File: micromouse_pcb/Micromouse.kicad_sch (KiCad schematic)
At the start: 83 parts, among them J1 Conn_01x06, J2 Conn_01x06, J3 SWD, J4 UART, Q1 NMOS, Q2 SFH300, Q3 SFH300, Q4 NMOS, Q5 SFH300, Q6 NMOS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

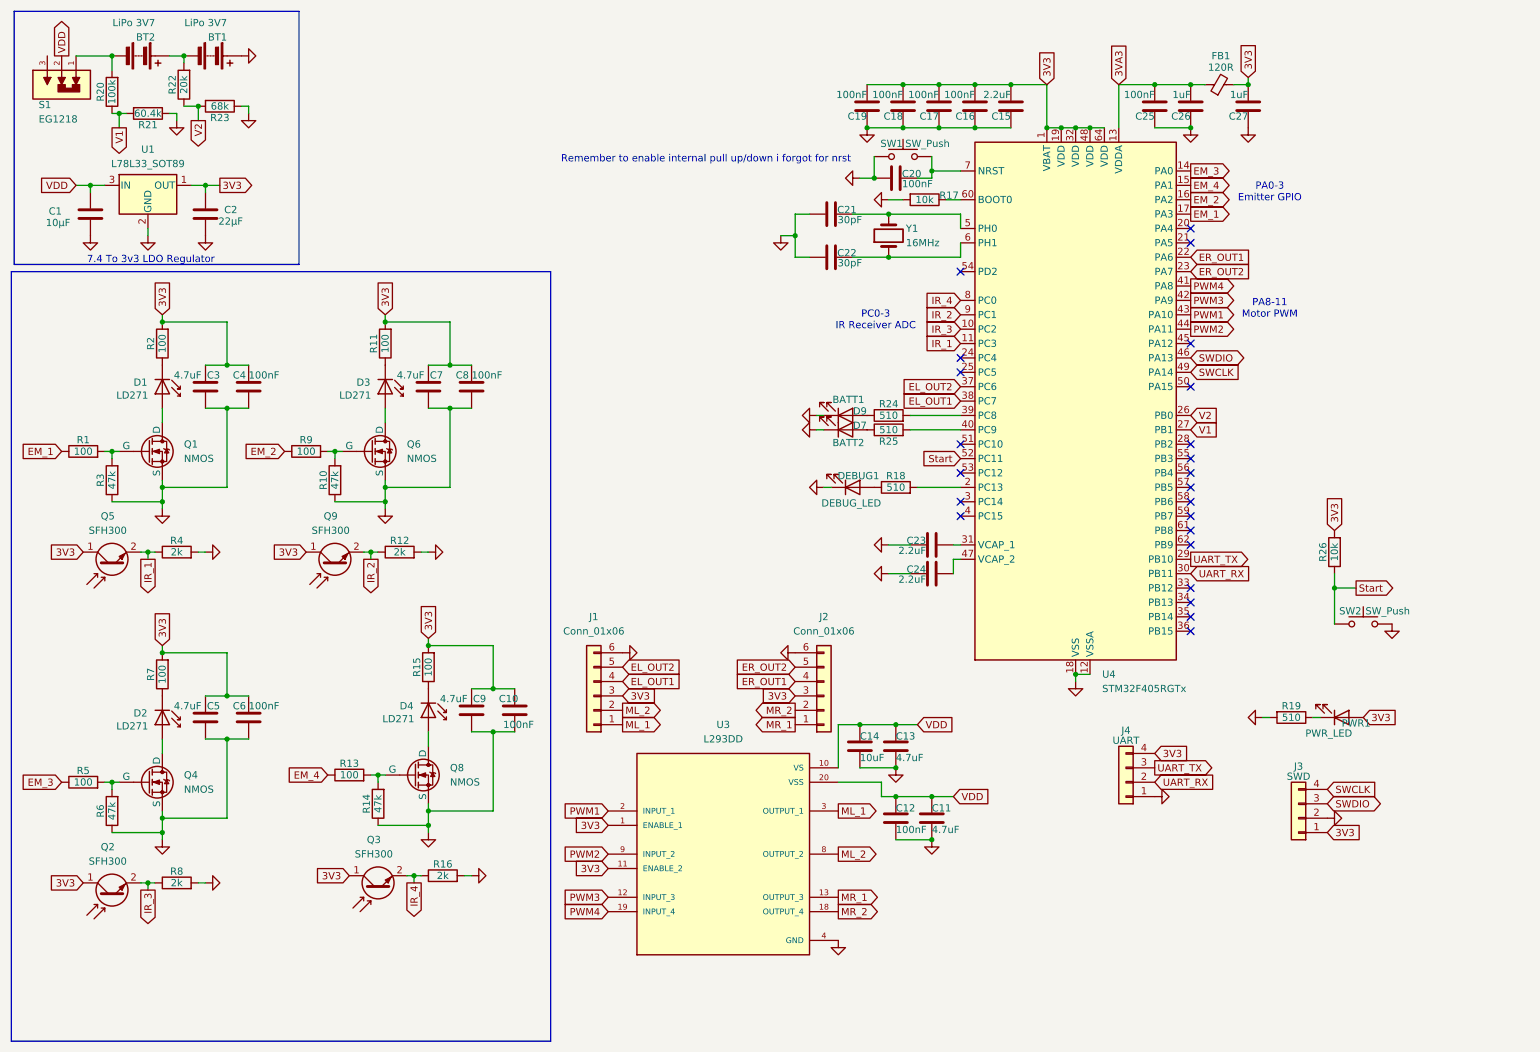
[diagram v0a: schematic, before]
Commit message: v2 kicad micromouse started, and turning is now possible but please fix distance reading and distance pids
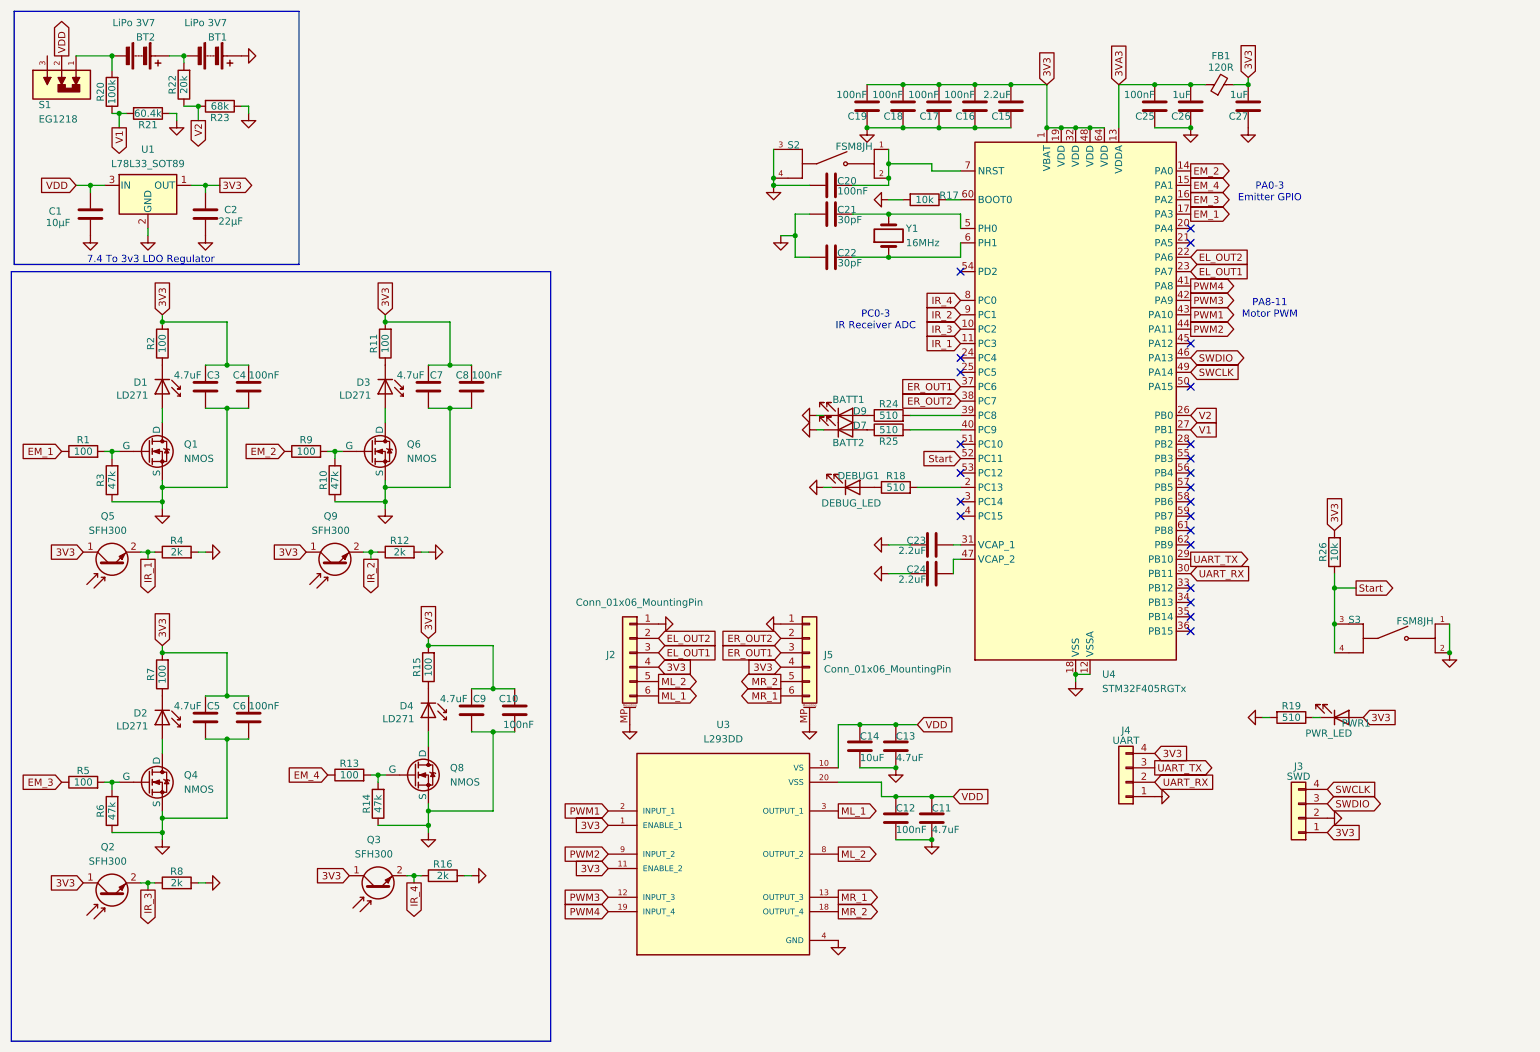
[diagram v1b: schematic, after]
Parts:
- removed J1, J2: Conn_01x06, Connector_JST:JST_SH_BM06B-SRSS-TB_1x06-1MP_P1.00mm_Vertical, symbol Connector_Generic:Conn_01x06
- removed SW1, SW2: SW_Push, footprints:SW4_1825910-B_TEC, symbol Switch:SW_Push
- added J2, J5: Conn_01x06_MountingPin, Connector_JST:JST_SH_BM06B-SRSS-TB_1x06-1MP_P1.00mm_Vertical, symbol Connector_Generic_MountingPin:Conn_01x06_MountingPin
- added S2, S3: FSM8JH, footprints:SW4_1825910-B_TEC, symbol FSM8JH:FSM8JH
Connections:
- net 3V3: now also J2.4 (Pin_4), J5.4 (Pin_4)
- net EL_OUT1: now also U4.23 (PA7), J2.3 (Pin_3); no longer U4.38 (PC7)
- net EL_OUT2: now also U4.22 (PA6), J2.2 (Pin_2); no longer U4.37 (PC6)
- net EM_2: now also U4.14 (PA0); no longer U4.16 (PA2)
- net EM_3: now also U4.16 (PA2); no longer U4.14 (PA0)
- net ER_OUT1: now also U4.37 (PC6), J5.3 (Pin_3); no longer U4.22 (PA6)
- net ER_OUT2: now also U4.38 (PC7), J5.2 (Pin_2); no longer U4.23 (PA7)
- net GND: now also J2.1 (Pin_1), J2.MP (MountPin), J5.1 (Pin_1), J5.MP (MountPin), S2.3, S2.4, S3.1, S3.2
- net ML_1: now also J2.6 (Pin_6)
- net ML_2: now also J2.5 (Pin_5)
- net MR_1: now also J5.6 (Pin_6)
- net MR_2: now also J5.5 (Pin_5)
- net Start: now also S3.3, S3.4
- net at C20.1, U4.7 (NRST): now also S2.1, S2.2
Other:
- note removed: "Remember to enable internal pull up/down i forgot for nrst"
- moved on the sheet: C20

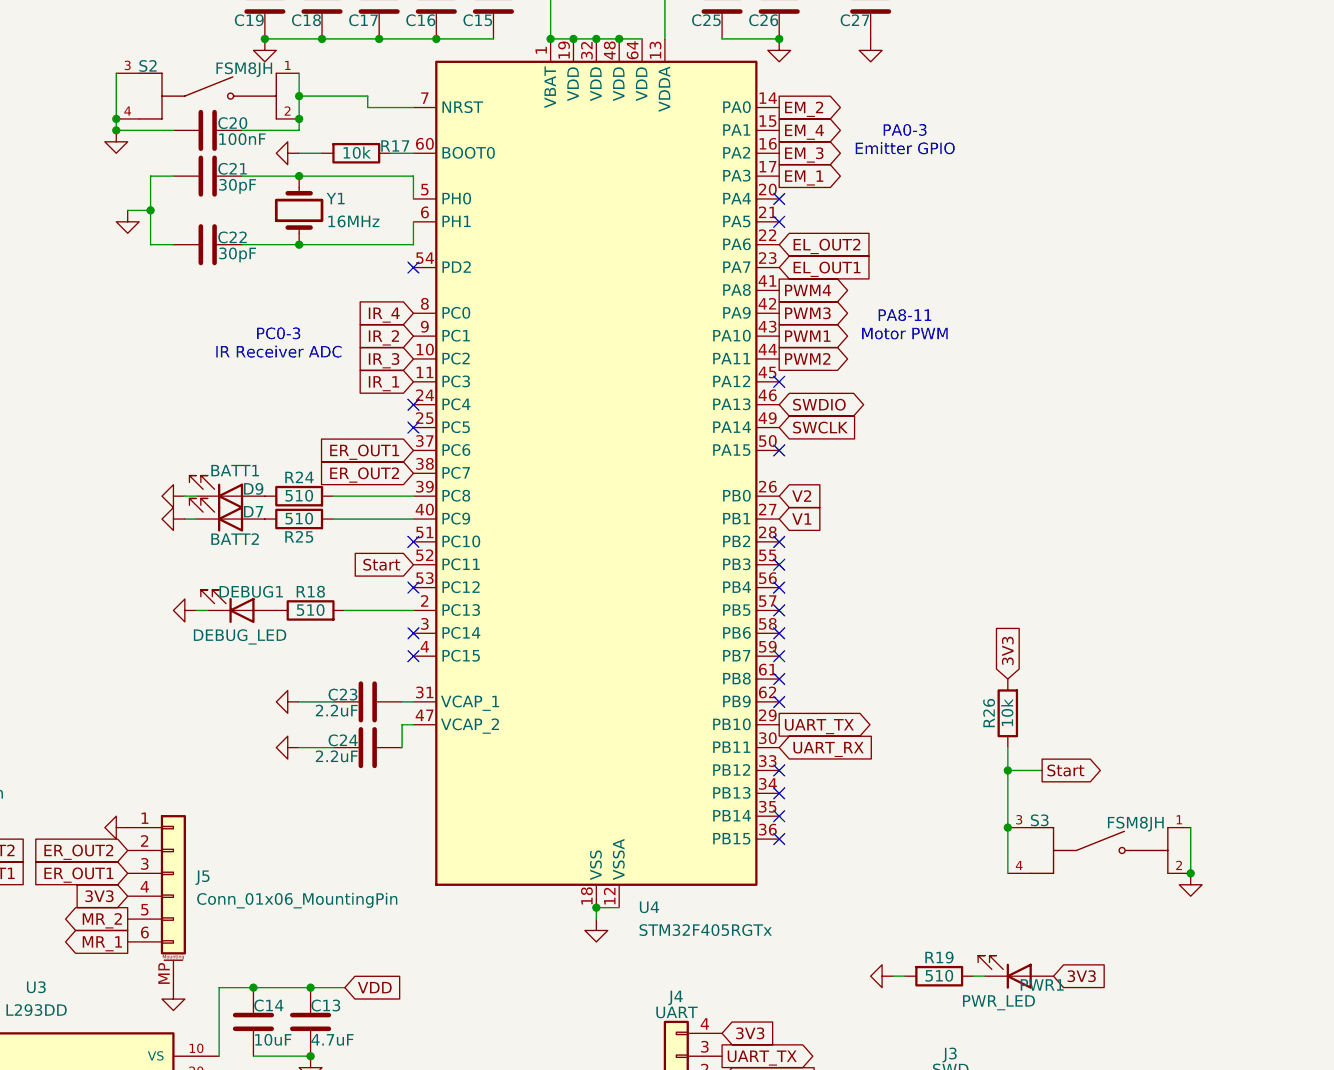
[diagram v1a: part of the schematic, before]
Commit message: finished v2 micromouse, finished move function, todo: fix distance pid
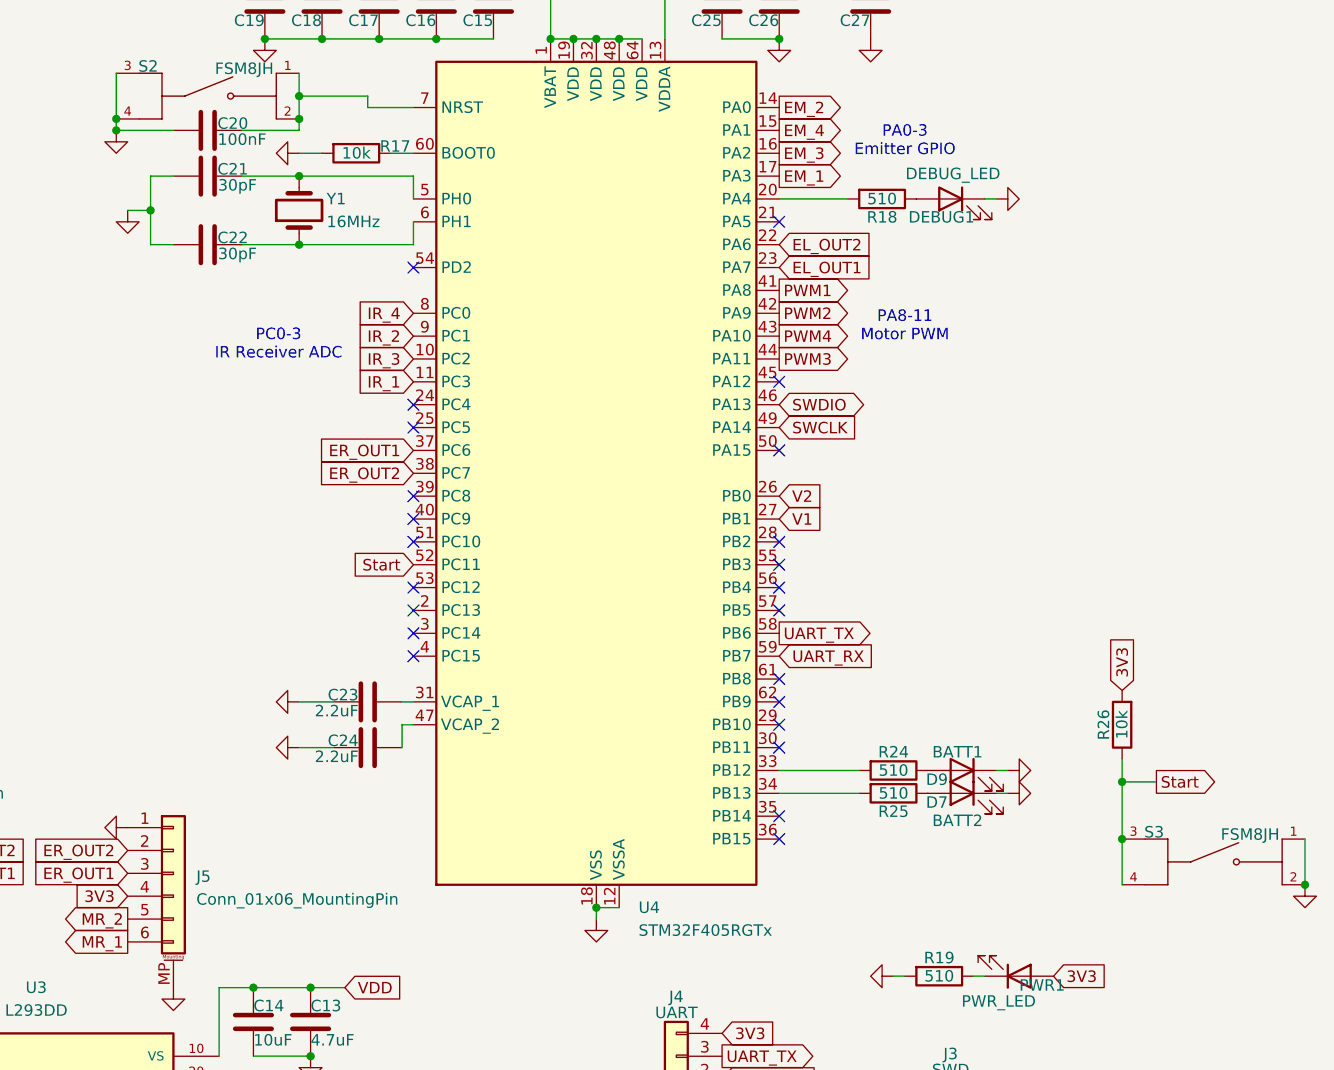
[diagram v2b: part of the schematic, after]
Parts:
- Q2, Q3, Q5, Q9: footprint LED_THT:led_micro -> micromouse:led_micro
- S1: DESCRIPTION Slide Switch SPDT Through Hole -> (none)
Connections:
- net PWM1: now also U4.41 (PA8); no longer U4.43 (PA10)
- net PWM2: now also U4.42 (PA9); no longer U4.44 (PA11)
- net PWM3: now also U4.44 (PA11); no longer U4.42 (PA9)
- net PWM4: now also U4.43 (PA10); no longer U4.41 (PA8)
- net UART_RX: now also U4.59 (PB7); no longer U4.30 (PB11)
- net UART_TX: now also U4.58 (PB6); no longer U4.29 (PB10)
- net at R24.2: now also U4.33 (PB12); no longer U4.39 (PC8)
- net at R18.2: now also U4.20 (PA4); no longer U4.2 (PC13)
- net at U4.34 (PB13): now also R25.2
- net at U4.40 (PC9): no longer R25.2
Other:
- moved on the sheet: D7, D9, DEBUG1, R18, R24, R25, R26, S3
